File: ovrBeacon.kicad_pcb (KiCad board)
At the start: 2 copper layers, 36.6 x 35.1 mm, 48 parts, among them J1 USB_MICROB_RA, J2 CONN_DBG_PDI, J3 CONN_2MM_9, Q1 FET_NP_5A/3A_60V, T1 THERM_NTC_10K_0603, U1 MICROCHIP_MCP73831, U10 WORLDSEMI_WS2812, U11 WORLDSEMI_WS2812, U12 WORLDSEMI_WS2812, U2 BLUEGIGA_BLE113, U3 TI_TPS62730, U4 WORLDSEMI_WS2812, U5 WORLDSEMI_WS2812, U6 WORLDSEMI_WS2812, U7 WORLDSEMI_WS2812, U8 TOSHIBA_TCS40DLR, U9 WORLDSEMI_WS2812

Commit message: initial commit of version 0.3…passed DFM, waiting for manufacture review
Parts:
- removed C14: C_0.1uF_10v_0603, ovrEngineered:C_0603
- removed J3: CONN_2MM_9, ovrEngineered:SIP_2MM_9
- removed Q1: FET_NP_5A/3A_60V, ovrEngineered:SO-8
- removed R13: R_15K_1%_0603, ovrEngineered:R_0603
- removed T1: THERM_NTC_10K_0603, ovrEngineered:R_0603
- removed U10, U11, U12, U9: WORLDSEMI_WS2812, ovrEngineered:WS2812
- removed U8: TOSHIBA_TCS40DLR, ovrEngineered:SOT-23-3
- added C1: C_0.15uF_25v_0603, ovrEngineered:C_0603, F.Cu at (141.2, 124.0)
- added C2: C_2200pF_50v_0603, ovrEngineered:C_0603, F.Cu at (138.2, 124.0)
- added C3: C_0.47uF_25v_0603, ovrEngineered:C_0603, F.Cu at (144.3, 120.7)
- added R18: R_120_1%_0603, ovrEngineered:R_0603, F.Cu at (144.0, 110.2)
- added R19: R_120_1%_0603, ovrEngineered:R_0603, F.Cu at (144.0, 109.0)
- C11, C13: value C_0.1uF_10v_0603 -> C_1uF_10v_0805; footprint ovrEngineered:C_0603 -> ovrEngineered:C_0805; moved to F.Cu
- C12: moved to F.Cu
- C4: value C_2.2uF_10v_0603 -> C_0.022uF_25v_0603
- C5: value C_2.2uF_10v_0603 -> C_10000pF_25v_0603
- C6: value C_0.1uF_10v_0603 -> C_10000pF_25v_0603
- C7: value C_0.1uF_10v_0603 -> C_0.022uF_25v_0603
- C8: value C_0.1uF_10v_0603 -> C_0.47uF_25v_0603
- C9: value C_0.47uF_10v_0603 -> C_22uF_25v_0805; footprint ovrEngineered:C_0603 -> ovrEngineered:C_0805
- D1: value LED_GREEN_0603 -> CREE_CLV1A_FKB; footprint ovrEngineered:D_0603 -> ovrEngineered:CREE_CLV1A_FKB
- D2: value LED_RED_0603 -> CREE_CLV1A_FKB; footprint ovrEngineered:D_0603 -> ovrEngineered:CREE_CLV1A_FKB
- J1: value USB_MICROB_RA -> CONN_1.27MM_5X2; footprint ovrEngineered:USB_MICROB_RA -> ovrEngineered:20021111-00010T4LF
- J2: value CONN_DBG_PDI -> CONN_2MM_2; footprint ovrEngineered:TC2030-IDC -> ovrEngineered:SIP_2MM_2
- L1: value I_2.2uH_20%_0603 -> QIRX_10.7uH; footprint ovrEngineered:R_0603 -> ovrEngineered:SIP_2MM_2
- R11: value R_402_1%_0603 -> R_12K_1%_0603
- R12: value R_10K_1%_0603 -> R_5.1K_1%_0603
- R14: value R_15K_1%_0603 -> R_120_1%_0603
- R15, R16: value R_10K_1%_0603 -> R_120_1%_0603
- R17: value R_402_1%_0603 -> R_120_1%_0603
- R3: value R_2K_1%_0603 -> R_953_1%_0603
- R4, R5: value R_5.1K_1%_0603 -> R_10K_1%_0603
- R6, R7: value R_10K_1%_0603 -> R_300_1%_0603
- R8: value R_15K_1%_0603 -> R_42.2K_1%_0603
- U1: value MICROCHIP_MCP73831 -> BLUEGIGA_BLE113; footprint ovrEngineered:SOT-23-5 -> ovrEngineered:BLE113
- U2: value BLUEGIGA_BLE113 -> TI_BQ51050; footprint ovrEngineered:BLE113 -> ovrEngineered:TI_BQ51050
- U3: value TI_TPS62730 -> TOREX_XC6210; footprint ovrEngineered:TPS62730 -> ovrEngineered:SOT-25-5
- U4: value WORLDSEMI_WS2812 -> NXP_PCA9624; footprint ovrEngineered:WS2812 -> ovrEngineered:NXP_PCA9624
- U5: value WORLDSEMI_WS2812 -> LITEON_LTR-329ALS; footprint ovrEngineered:WS2812 -> ovrEngineered:LITEON_LTR-329ALS; moved to F.Cu
- U6: value WORLDSEMI_WS2812 -> SILICONLABS_SI7050; footprint ovrEngineered:WS2812 -> ovrEngineered:SILICONLABS_SI7050
- U7: value WORLDSEMI_WS2812 -> ANALOGDEVS_ADXL345; footprint ovrEngineered:WS2812 -> ovrEngineered:ANALOGDEVS_ADXL345; moved to F.Cu
- moved U2 87.8 mm to (139.7, 120.2), turned to 90 degrees
- moved L1 86.1 mm to (140.7, 125.7), turned to 180 degrees
- moved C5 85.3 mm to (144.3, 121.9)
- moved C10 83.0 mm to (141.5, 114.3)
- moved R8 77.9 mm to (131.8, 118.4)
- moved U5 76.5 mm to (136.4, 102.0), turned to 90 degrees
- moved R12 76.5 mm to (145.5, 114.3), turned to 90 degrees
- moved R9 75.9 mm to (144.0, 105.9)
- moved U3 75.5 mm to (138.7, 114.3), turned to 0 degrees
- moved C6 74.3 mm to (136.1, 121.9), turned to 270 degrees
- moved R4 71.9 mm to (144.3, 118.1), turned to 0 degrees
- moved C13 71.8 mm to (134.4, 114.0), turned to 90 degrees
- moved R11 71.5 mm to (142.7, 114.3)
- moved R3 68.7 mm to (144.3, 116.8)
- moved U4 68.1 mm to (139.7, 108.7)
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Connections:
- C10 pad 1: +BATT -> +3V3
- C11 pad 1: +BATT -> +3V3
- C4 pad 1: +BATT -> Net-(C1-Pad2)
- C4 pad 2: GND -> Net-(C4-Pad2)
- C5 pad 1: VCC -> Net-(C1-Pad2)
- C5 pad 2: GND -> Net-(C5-Pad2)
- C6 pad 1: +BATT -> Net-(C2-Pad2)
- C6 pad 2: GND -> Net-(C6-Pad2)
- C7 pad 1: +BATT -> Net-(C2-Pad2)
- C7 pad 2: GND -> Net-(C7-Pad2)
- C8 pad 1: +BATT -> Net-(C2-Pad2)
- C8 pad 2: GND -> Net-(C8-Pad2)
- C9 pad 1: +BATT -> Net-(C9-Pad1)
- D1 pad 1: +BATT -> Net-(D1-Pad1)
- D1 pad 2: Net-(D1-Pad2) -> +3V3
- D2 pad 2: Net-(D2-Pad2) -> +3V3
- J1 pad 1: Net-(J1-Pad1) -> GND
- J1 pad 2: (no net) -> +3V3
- J1 pad 3: (no net) -> /P2_2/PROG
- J1 pad 4: (no net) -> /P2_1/PROG
- J1 pad 5: GND -> (no net)
- J2 pad 1: /P2_1/PROG -> GND
- J2 pad 2: VCC -> +BATT
- L1 pad 1: Net-(L1-Pad1) -> Net-(C1-Pad1)
- L1 pad 2: VCC -> Net-(C2-Pad2)
- R1 pad 1: VCC -> +3V3
- R10 pad 1: Net-(Q1-Pad4) -> +3V3
- R10 pad 2: +BATT -> /SCL
- R11 pad 1: Net-(D1-Pad2) -> +BATT
- R11 pad 2: Net-(Q1-Pad4) -> /VBATT
- R12 pad 1: /EXT_POWER -> /VBATT
- R14 pad 1: /THERM_INT -> Net-(R14-Pad1)
- R14 pad 2: GND -> Net-(D1-Pad1)
- R15 pad 1: /NEOPIXELS -> Net-(R15-Pad1)
- R15 pad 2: GND -> Net-(D1-Pad4)
- R16 pad 1: GND -> Net-(R16-Pad1)
- R16 pad 2: /SW_ENUM -> Net-(D1-Pad3)
- R17 pad 1: Net-(D2-Pad2) -> Net-(R17-Pad1)
- R17 pad 2: GND -> Net-(D2-Pad1)
- R4 pad 1: Net-(J1-Pad1) -> +3V3
- R4 pad 2: /CHARGING -> /~CHARGING
- R5 pad 1: /CHARGING_STAT -> Net-(R5-Pad1)
- R5 pad 2: Net-(R5-Pad2) -> GND
- R6 pad 1: GND -> Net-(R6-Pad1)
- R6 pad 2: /CHARGING_STAT -> GND
- R7 pad 1: /CHARGING -> Net-(R6-Pad1)
- R7 pad 2: GND -> Net-(R7-Pad2)
- R8 pad 1: /THERM_EXT_1 -> Net-(C9-Pad1)
- R8 pad 2: GND -> Net-(R6-Pad1)
- R9 pad 1: /DCDC -> +3V3
- R9 pad 2: GND -> /SDA
- U1 pad 1: Net-(R5-Pad2) -> GND
- U1 pad 3: +BATT -> GND
- U1 pad 4: Net-(J1-Pad1) -> GND
- U1 pad 5: Net-(R3-Pad1) -> GND
- U2 pad 10: /P2_1/PROG -> Net-(R3-Pad1)
- U2 pad 11: /THERM_EXT_1 -> +BATT
- U2 pad 12: /THERM_EXT_2 -> Net-(R7-Pad2)
- U2 pad 13: /DCDC -> Net-(R5-Pad1)
- U2 pad 14: (no net) -> Net-(R6-Pad1)
- U2 pad 15: (no net) -> Net-(C7-Pad2)
- U2 pad 16: (no net) -> Net-(C8-Pad2)
- U2 pad 17: VCC -> Net-(C6-Pad2)
- U2 pad 18: GND -> Net-(C9-Pad1)
- U2 pad 19: /EXT_POWER -> Net-(C2-Pad2)
- U2 pad 2: GND -> Net-(C1-Pad2)
- U2 pad 20: /CHARGING -> GND
- U2 pad 21: /SW_ENUM -> GND
- U2 pad 3: GND -> Net-(C5-Pad2)
- U2 pad 4: GND -> +BATT
- U2 pad 5: GND -> Net-(C3-Pad2)
- U2 pad 6: GND -> Net-(C4-Pad2)
- U2 pad 7: GND -> /~CHARGING
- U2 pad 8: VCC -> (no net)
- U2 pad 9: /P2_2/PROG -> GND
- U3 pad 1: (no net) -> +BATT
- U3 pad 2: Net-(L1-Pad1) -> GND
- U3 pad 4: GND -> (no net)
- U3 pad 5: /DCDC -> +3V3
- U4 pad 1: +BATT -> +3V3
- U4 pad 2: Net-(U4-Pad2) -> +3V3
- U4 pad 4: /NEOPIXELS -> GND
- U5 pad 1: +BATT -> +3V3
- U5 pad 2: Net-(U5-Pad2) -> GND
- U5 pad 3: GND -> /SDA
- U5 pad 4: Net-(U11-Pad2) -> /SCL
- U6 pad 1: +BATT -> /SDA
- U6 pad 2: Net-(U6-Pad2) -> GND
- U6 pad 3: GND -> (no net)
- U6 pad 4: Net-(U4-Pad2) -> (no net)
- U7 pad 1: +BATT -> +3V3
- U7 pad 2: Net-(U10-Pad4) -> GND
- U7 pad 3: GND -> (no net)
- U7 pad 4: Net-(U5-Pad2) -> GND
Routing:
- net +BATT: track 131.7 -> 23.0 mm, vias 16 -> 2
- net +3V3: track 0.00 -> 101.3 mm, vias 0 -> 10
- net GND: track 111.5 -> 48.8 mm, vias 22 -> 18
- net VCC: track 53.8 -> 0.00 mm, vias 4 -> 0
- net Net-(U10-Pad4): track 30.1 -> 0.00 mm
- net Net-(U4-Pad2): track 29.6 -> 0.00 mm
- net Net-(U11-Pad4): track 29.0 -> 0.00 mm, vias 2 -> 0
- net Net-(U10-Pad2): track 28.3 -> 0.00 mm
- net Net-(U5-Pad2): track 28.3 -> 0.00 mm
- net /SCL: track 0.00 -> 25.9 mm, vias 0 -> 4
- net /SDA: track 0.00 -> 21.7 mm, vias 0 -> 2
- net /VBATT: track 0.00 -> 20.8 mm, vias 0 -> 2
- net /TIMER1_CC0/ADC: track 19.8 -> 0.00 mm, vias 1 -> 0
- net /THERM_EXT_2: track 19.5 -> 0.00 mm, vias 1 -> 0
- net /~CHARGING: track 0.00 -> 18.0 mm, vias 0 -> 2
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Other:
- board size 36.6 x 35.1 mm -> 17.3 x 38.4 mm
- board text added: "Battery Outline"
- board text added: "v0.3 ovrBeacon Jan 2017"
- board text removed: "A+T"
- board text removed: "BAT"
- board text removed: "ERR"
- board text removed: "GND"
- board text removed: "T1"
- board text removed: "T2"
- board text removed: "VCC"
- board text removed: "VSW"
- board text removed: "ovrBeacon v0.1 ovrEngineered, LLC July 2016"

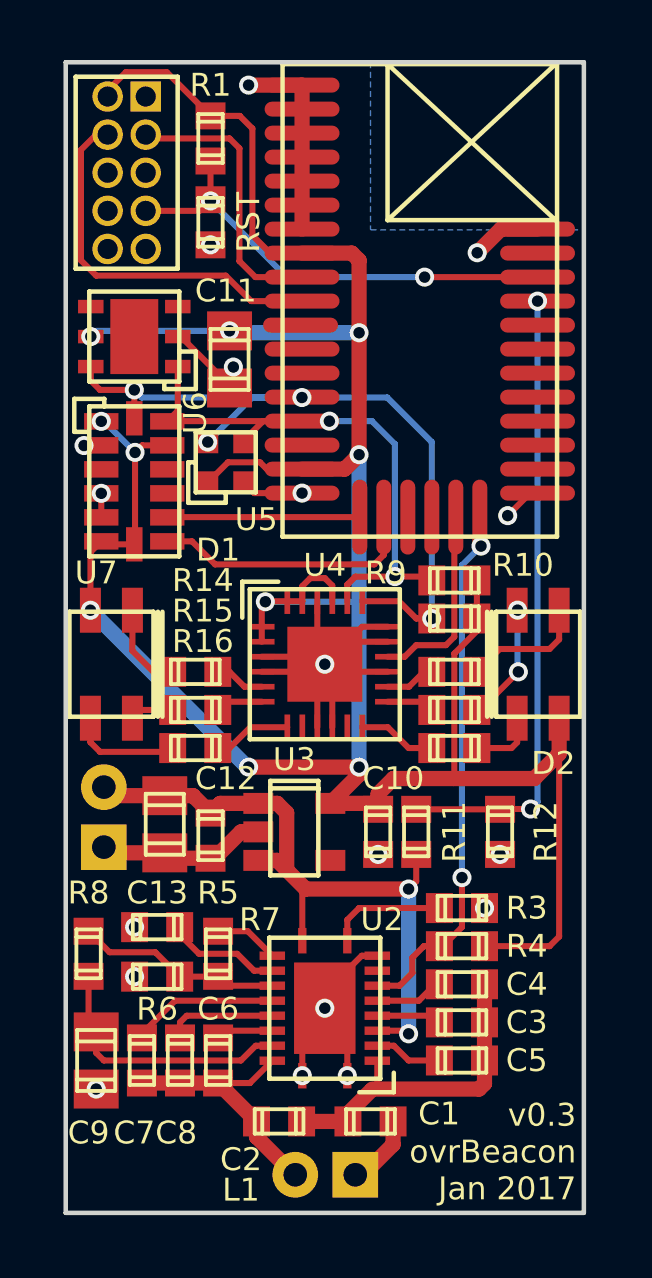
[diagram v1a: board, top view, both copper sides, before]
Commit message: Fixed redlines from v0.3, added fiducials for pick and place…getting ready to start adjusting component centers for pick and place
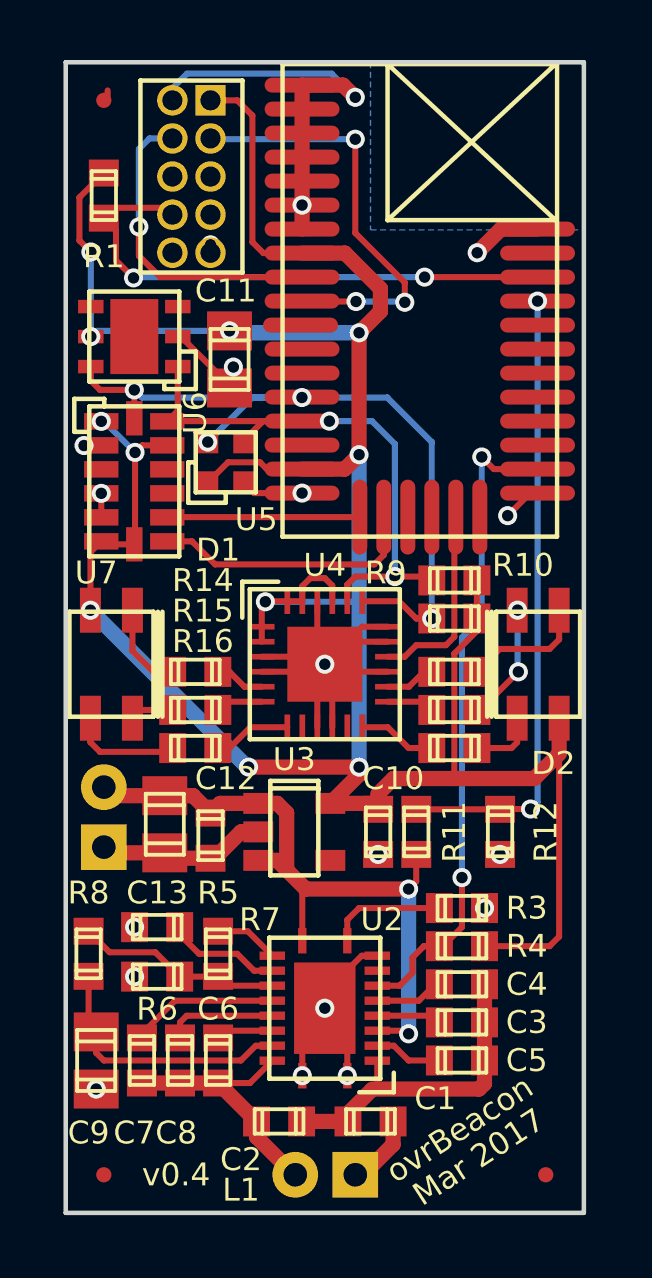
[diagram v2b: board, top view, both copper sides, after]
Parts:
- removed R2: R_0_0603, ovrEngineered:R_0603
- added REF**: fiducial, ovrEngineered:fiducial, F.Cu at (132.3, 89.9)
- added REF**: fiducial, ovrEngineered:fiducial, F.Cu at (132.6, 125.7)
- added REF**: fiducial, ovrEngineered:fiducial, F.Cu at (147.1, 125.7)
- moved R1 4.03 mm to (132.3, 93.1)
- moved J1 2.16 mm to (135.3, 92.5)
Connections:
- J1 pad 1: GND -> +3V3
- J1 pad 2: +3V3 -> GND
- J1 pad 3: /P2_2/PROG -> /P2_1/PROG
- J1 pad 4: /P2_1/PROG -> /P2_2/PROG
- J1 pad 7: /~RESET -> (no net)
- J1 pad 8: (no net) -> /~RESET
- U1 pad 24: /~CHARGING -> (no net)
- U1 pad 26: (no net) -> /~CHARGING
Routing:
- net GND: track 48.8 -> 56.0 mm
- net /~CHARGING: track 18.0 -> 22.0 mm
- net +3V3: track 101.3 -> 104.8 mm, vias 10 -> 11
- net /~RESET: track 15.9 -> 18.7 mm
- net /P2_1/PROG: track 12.7 -> 14.4 mm, vias 0 -> 3
- net /P2_2/PROG: track 9.74 -> 10.6 mm, vias 0 -> 1
- net (no net): track 0.00 -> 0.20 mm, vias 0 -> 1
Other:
- board text added: "Mar 2017"
- board text added: "ovrBeacon"
- board text added: "v0.4"
- board text removed: "RST"
- board text removed: "v0.3 ovrBeacon Jan 2017"

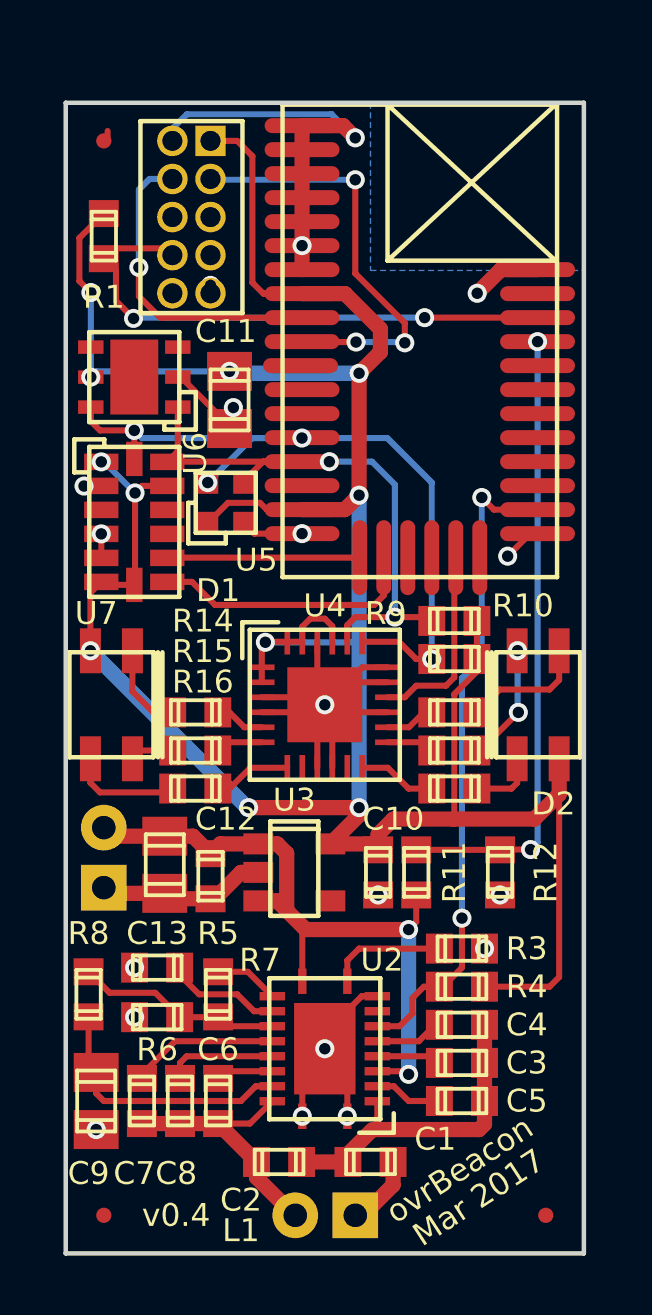
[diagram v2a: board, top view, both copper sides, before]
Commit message: Adjusted component centers and orientation for pick and place
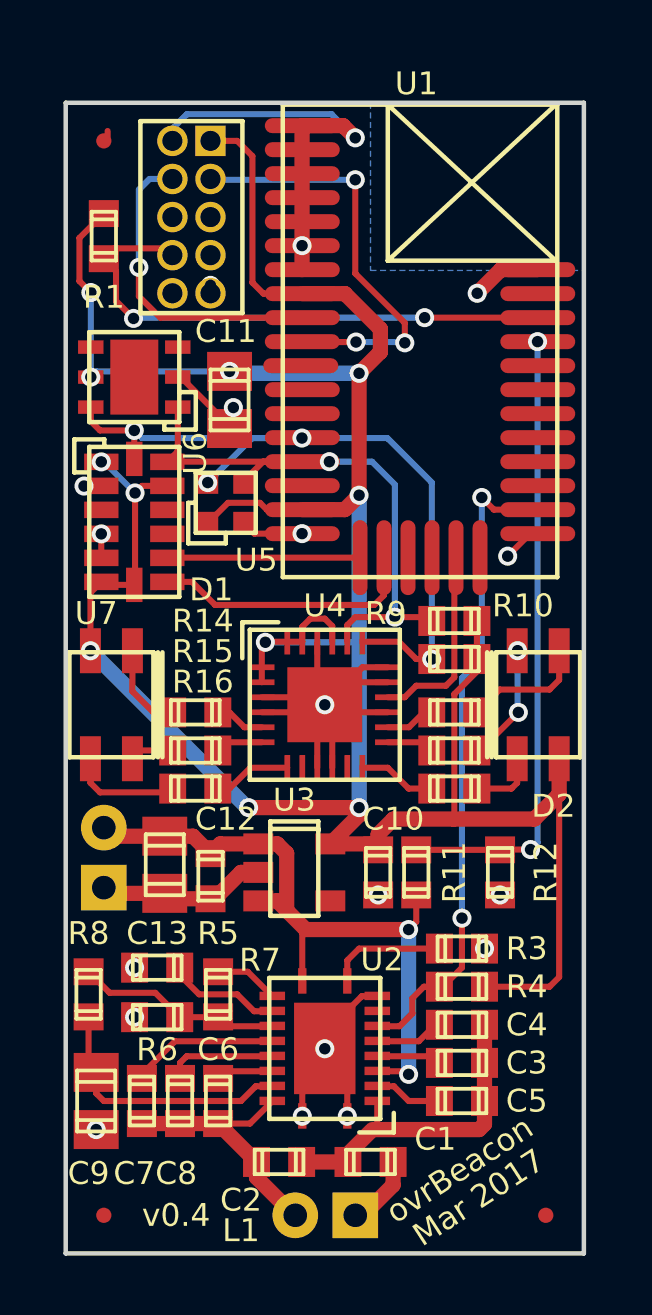
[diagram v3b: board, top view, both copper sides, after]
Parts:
- moved U1 8.08 mm to (142.9, 96.6)
- turned U2 to 180 degrees
- turned D1 to 0 degrees
- turned D2 to 180 degrees

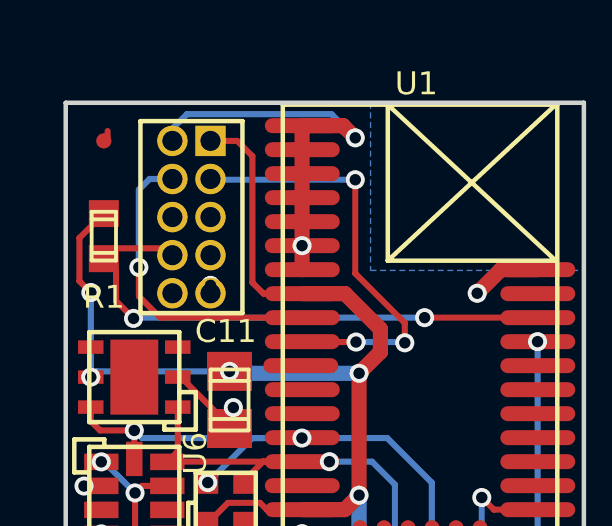
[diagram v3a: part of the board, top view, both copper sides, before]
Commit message: ready for fabrication w/ fiducials, redlines from v0.3, and pick and place file
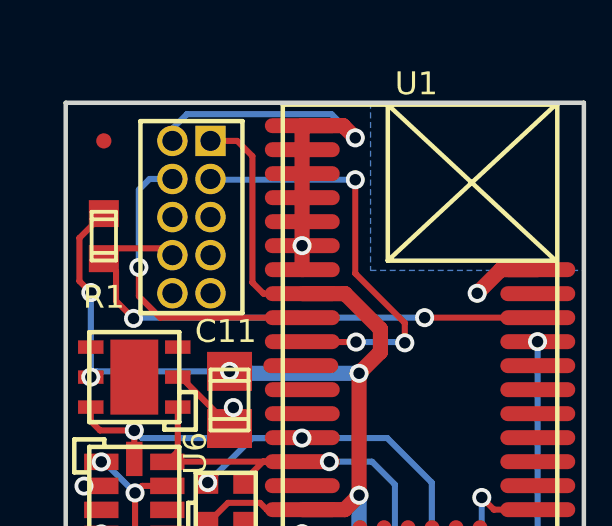
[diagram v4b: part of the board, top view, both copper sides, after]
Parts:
- removed REF**: fiducial, ovrEngineered:fiducial
- added FID1: fiducial, ovrEngineered:fiducial, F.Cu at (132.3, 125.7)
- renumbered REF** to FID2, REF** to FID3
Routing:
- net (no net): track 0.20 -> 0.00 mm, vias 1 -> 0
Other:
- rule pad_to_mask_clearance: 0.2 -> 0.1524
